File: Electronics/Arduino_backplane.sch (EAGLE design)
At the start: 36 parts, among them IC1 4013N, IC2 MCP4802, IC3 MCP4802, Q1 BF199, Q5 BF199, X1 M25-HD-20, X2 M25-HD-20

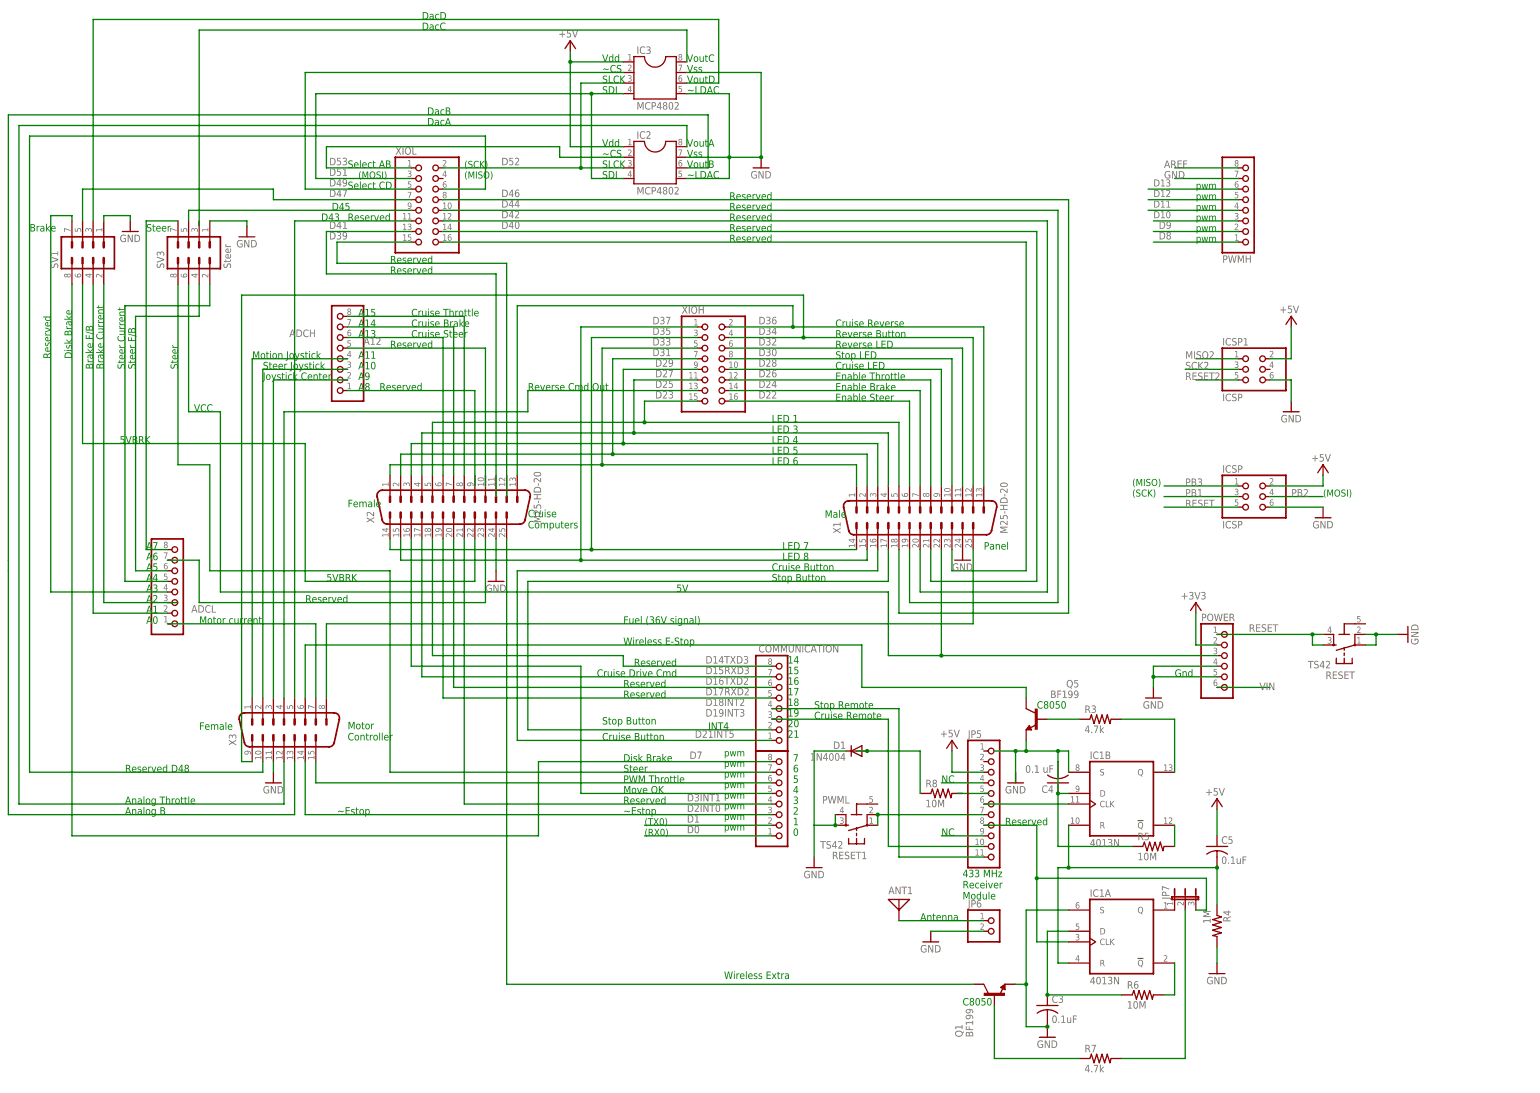
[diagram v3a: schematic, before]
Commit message: Reduced warnings; 97% routed.
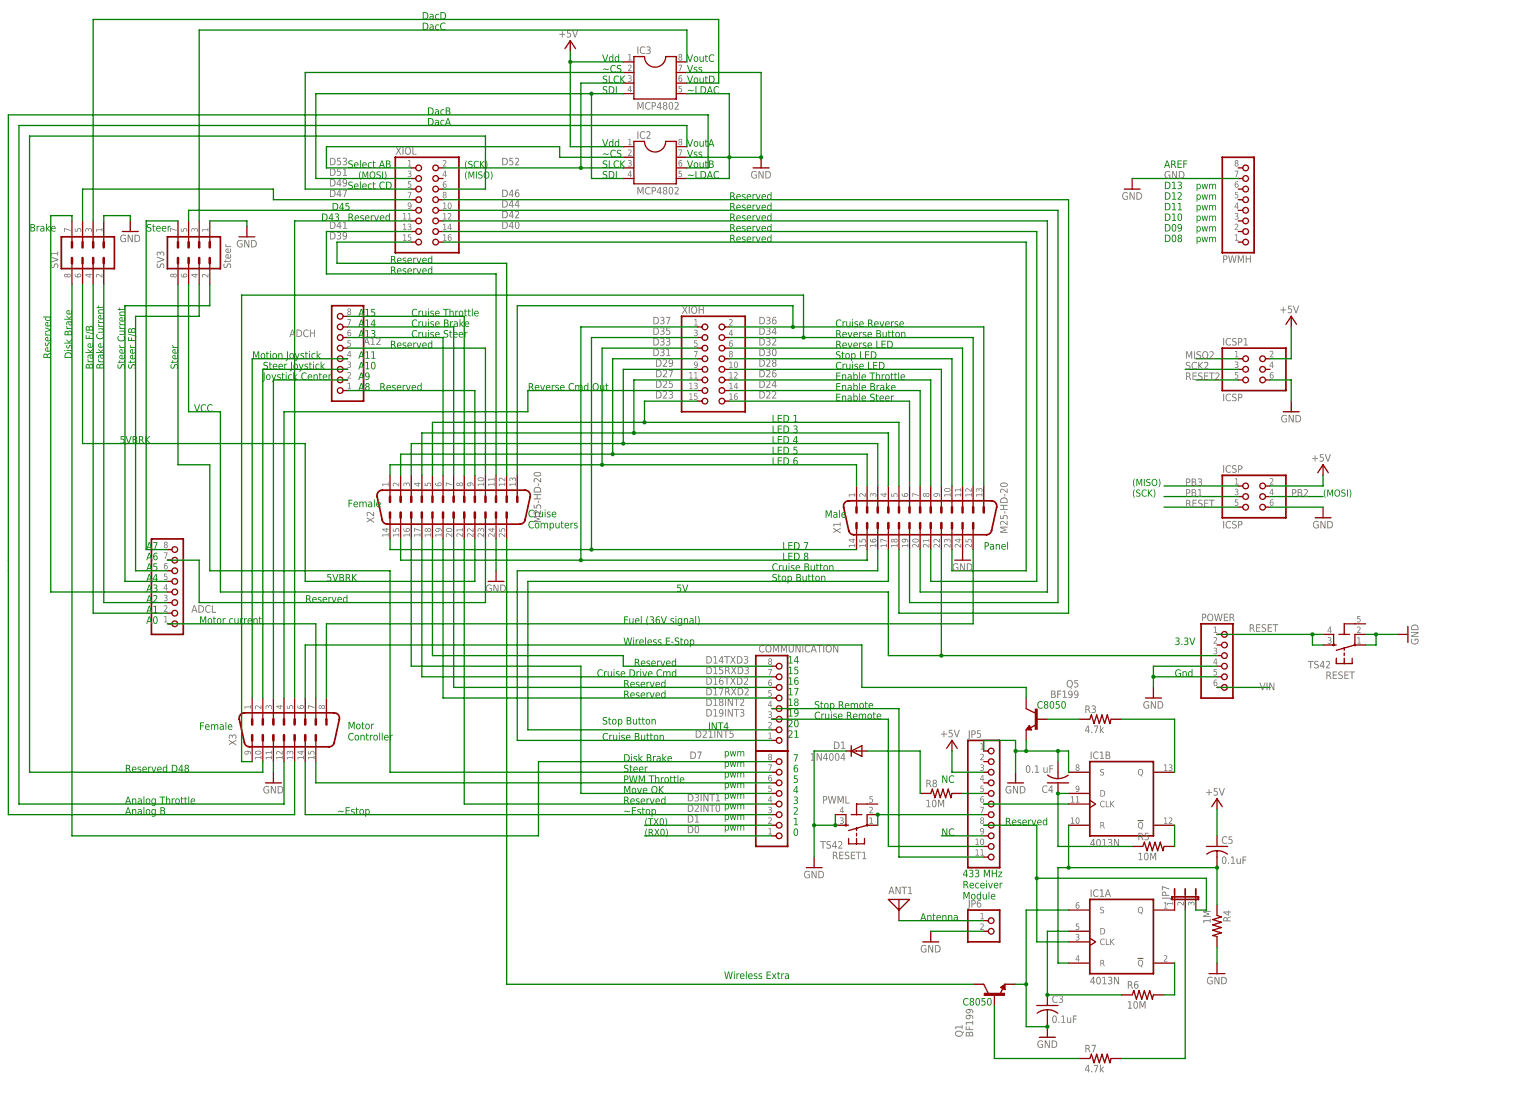
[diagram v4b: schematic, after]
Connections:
- removed net +3V3: POWER.2
- removed net AREF: PWMH.8
- removed net D10: PWMH.3
- removed net D11: PWMH.4
- removed net D12: PWMH.5
- removed net D13: PWMH.6
- removed net D8: PWMH.1
- removed net D9: PWMH.2
- removed net N$11: C4.1, C4.2, IC1B.D, IC1B.S, Q5.E, R5.1
- new net N$3: JP5.5, R8.2
- net A12: now also X2.10
- net D23: now also ADCH.1, X2.9
- net D39: now also X2.12
- net D41: now also X2.11
- net DACC: now also SV3.3
- net GND: now also C4.2, IC1B.S, JP5.1, Q5.E
- net N$1: now also ADCL.3
- net N$2: now also C4.1, IC1B.D, R5.1; no longer ADCH.1
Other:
- note added: "3.3V"
- note added: "AREF"
- note added: "D08"
- note added: "D09"
- note added: "D10"
- note added: "D11"
- note added: "D12"
- note added: "D13"

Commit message: Modifications by Tyler and Charles on March 14.
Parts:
- removed IC1: 4013N, 40xx:4013N
- added IC4: 4013N, ic-package:DIL14
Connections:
- removed net N$2: C4.1, IC1B.D, R5.1
- removed net N$25: IC1B.CLK, JP5.6
- removed net N$27: JP7.2, R7.2
- removed net N$30: IC1A.CLK, JP5.8, JP7.3
- removed net N$34: IC1B.!Q, R5.2
- removed net N$35: C3.1, IC1A.D, R6.1
- removed net N$36: C5.2, IC1A.R, IC1B.R, R4.1
- removed net N$38: IC1A.!Q, R6.2
- removed net N$39: Q1.B, R7.1
- removed net N$4: IC1A.Q, JP7.1
- removed net N$5: IC1B.Q, R3.2
- new net CLKA: IC4.3, JP5.8, JP7.3
- new net CLKB: IC4.11, JP5.6
- new net DA: C3.1, IC4.5, R6.1
- new net DB: C4.1, IC4.9, R5.1
- new net N$11: JP7.2, R7.1
- new net N$12: Q1.B, R7.2
- new net QA: IC4.1, JP7.1
- new net QB: R3.2
- new net RA: C5.2, IC4.10, IC4.4, R4.1
- new net ~QA: IC4.2, R6.2
- new net ~QB: IC4.12, R5.2
- net +5V: now also IC4.14
- net GND: now also IC4.6, IC4.7, IC4.8; no longer IC1A.S, IC1B.S
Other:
- note added: "CLKB"
- note added: "ClkA"
- note added: "DA"
- note added: "DB"
- note added: "QA"
- note added: "QB"
- note added: "RA"
- note added: "RB"
- note added: "SA"
- note added: "SB"
- note added: "~QA"
- note added: "~QB"
- moved on the sheet: C3, C4, C5, JP7, Q1, Q5, R3, R4, R5, R6, R7
